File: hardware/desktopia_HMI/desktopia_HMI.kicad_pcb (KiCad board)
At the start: 2 copper layers, 142.2 x 20 mm, 12 parts, among them J1 LCD_Connector, SW1 SW_Push, SW2 SW_Push, SW3 SW_Push, SW4 SW_Push, SW5 SW_Push

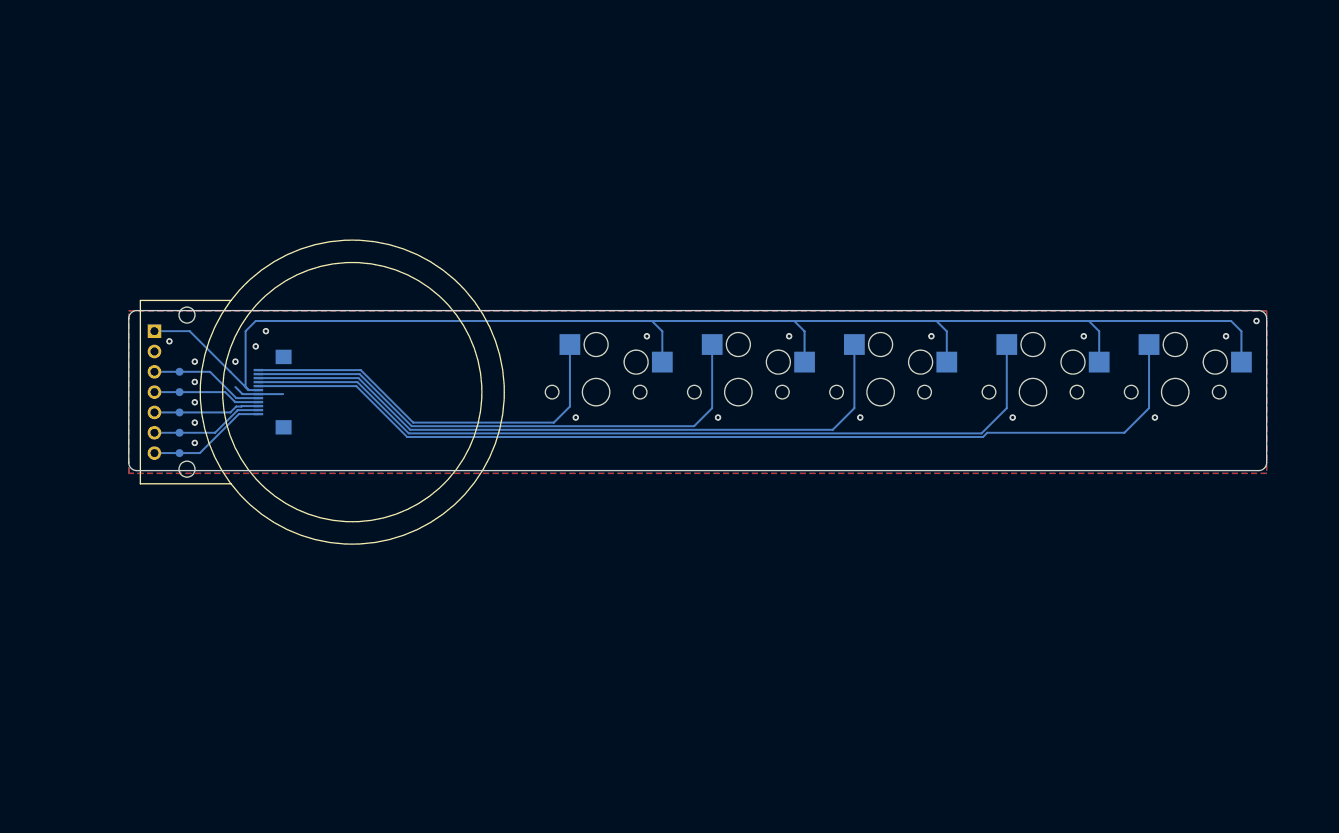
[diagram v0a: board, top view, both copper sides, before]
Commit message: hardware: HMI board re-annotated, PCB updated from the RP2040 schematic
The PCB now holds the RP2040 design (references included); the routing is not finished. README tables, connector pin-outs, test points and assembly notes follow the new references.

Co-Authored-By: Claude Opus 5.5 <noreply@anthropic.com>
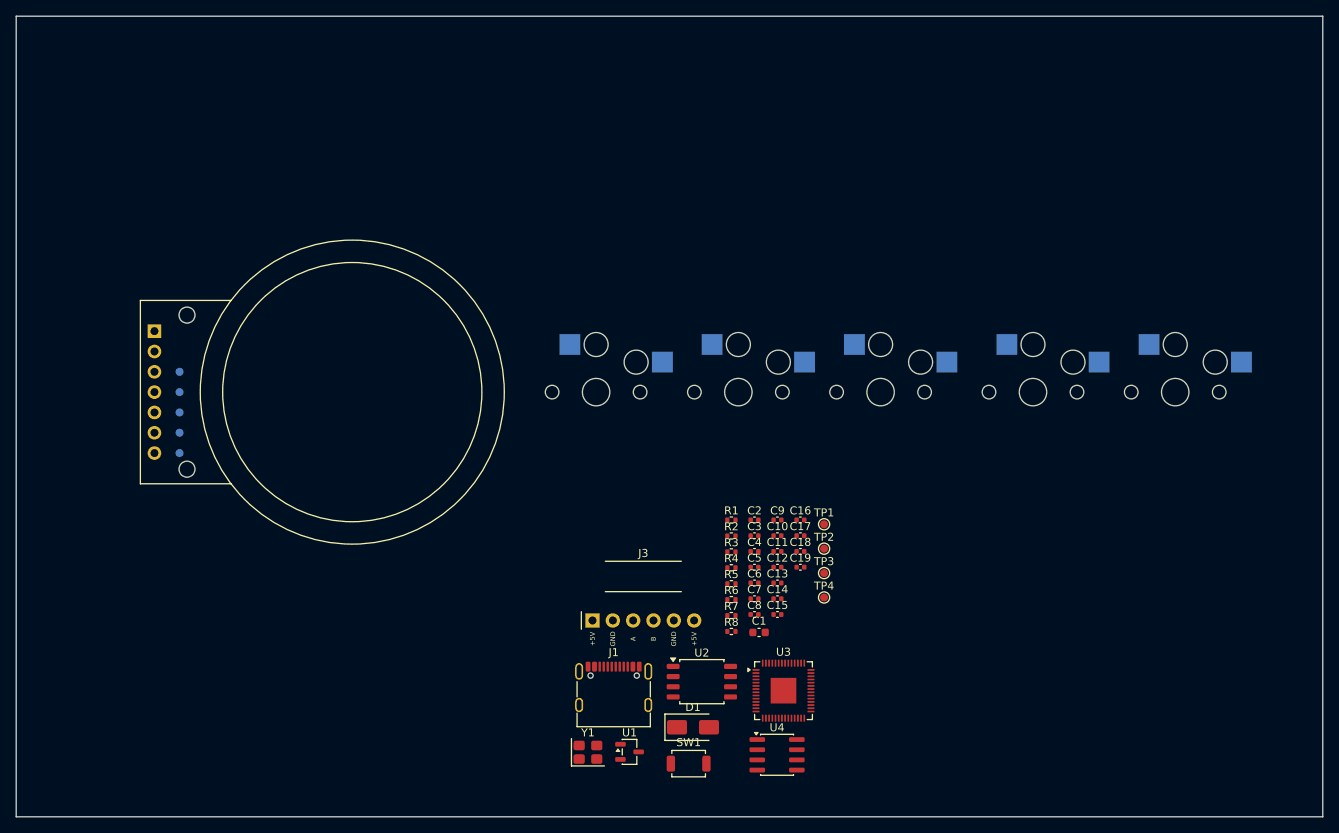
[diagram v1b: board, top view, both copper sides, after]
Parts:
- removed FPC_HMI1: F2D12U-A1G1-ER, JLCImport:F2D12U-A1G1-ER
- added C1: 10uF, Capacitor_SMD:C_0603_1608Metric, F.Cu at (138.6, 117.7)
- added C10: 33pF, Capacitor_SMD:C_0402_1005Metric, F.Cu at (140.9, 105.6)
- added C11: 100nF, Capacitor_SMD:C_0402_1005Metric, F.Cu at (140.9, 107.5)
- added C12: 100nF, Capacitor_SMD:C_0402_1005Metric, F.Cu at (140.9, 109.5)
- added C13: 100nF, Capacitor_SMD:C_0402_1005Metric, F.Cu at (140.9, 111.5)
- added C14: 1uF, Capacitor_SMD:C_0402_1005Metric, F.Cu at (140.9, 113.5)
- added C15: 100nF, Capacitor_SMD:C_0402_1005Metric, F.Cu at (140.9, 115.4)
- added C16: 1uF, Capacitor_SMD:C_0402_1005Metric, F.Cu at (143.7, 103.6)
- added C17: 100nF, Capacitor_SMD:C_0402_1005Metric, F.Cu at (143.7, 105.6)
- added C18: 100nF, Capacitor_SMD:C_0402_1005Metric, F.Cu at (143.7, 107.5)
- added C19: 100nF, Capacitor_SMD:C_0402_1005Metric, F.Cu at (143.7, 109.5)
- added C2: 1uF, Capacitor_SMD:C_0402_1005Metric, F.Cu at (138.0, 103.6)
- added C3: 1uF, Capacitor_SMD:C_0402_1005Metric, F.Cu at (138.0, 105.6)
- added C4: 100nF, Capacitor_SMD:C_0402_1005Metric, F.Cu at (138.0, 107.5)
- added C5: 100nF, Capacitor_SMD:C_0402_1005Metric, F.Cu at (138.0, 109.5)
- added C6: 100nF, Capacitor_SMD:C_0402_1005Metric, F.Cu at (138.0, 111.5)
- added C7: 100nF, Capacitor_SMD:C_0402_1005Metric, F.Cu at (138.0, 113.5)
- added C8: 33pF, Capacitor_SMD:C_0402_1005Metric, F.Cu at (138.0, 115.4)
- added C9: 100nF, Capacitor_SMD:C_0402_1005Metric, F.Cu at (140.9, 103.6)
- added D1: SS14, Diode_SMD:D_SMA, F.Cu at (130.3, 129.5)
- added J1: GT-USB-7010ASV, Connector_USB:USB_C_Receptacle_G-Switch_GT-USB-7010ASV, F.Cu at (120.4, 125.7)
- added J3: 6P6C cord, soldered, Desktopia:Cable_6P6C_SolderPads, F.Cu at (124.1, 116.2)
- added R1: 5.1k, Resistor_SMD:R_0402_1005Metric, F.Cu at (135.1, 103.6)
- added R2: 22, Resistor_SMD:R_0402_1005Metric, F.Cu at (135.1, 105.6)
- added R3: 5.1k, Resistor_SMD:R_0402_1005Metric, F.Cu at (135.1, 107.6)
- added R4: 22, Resistor_SMD:R_0402_1005Metric, F.Cu at (135.1, 109.6)
- added R5: 1k, Resistor_SMD:R_0402_1005Metric, F.Cu at (135.1, 111.6)
- added R6: 1k, Resistor_SMD:R_0402_1005Metric, F.Cu at (135.1, 113.6)
- added R7: 10k, Resistor_SMD:R_0402_1005Metric, F.Cu at (135.1, 115.6)
- added R8: 120, Resistor_SMD:R_0402_1005Metric, F.Cu at (135.1, 117.5)
- added SW1: TS-1088-AR02016, Button_Switch_SMD:SW_SPST_TS-1088-xR020, F.Cu at (129.8, 134.1)
- added TP1: TestPoint, TestPoint:TestPoint_Pad_D1.0mm, F.Cu at (146.7, 104.1)
- added TP2: TestPoint, TestPoint:TestPoint_Pad_D1.0mm, F.Cu at (146.7, 107.2)
- added TP3: TestPoint, TestPoint:TestPoint_Pad_D1.0mm, F.Cu at (146.7, 110.2)
- added TP4: TestPoint, TestPoint:TestPoint_Pad_D1.0mm, F.Cu at (146.7, 113.3)
- added U1: XC6206P332MR, Package_TO_SOT_SMD:SOT-23-3, F.Cu at (122.4, 132.6)
- added U2: W25Q128JVSIQ, Package_SO:SOIC-8_5.3x5.3mm_P1.27mm, F.Cu at (131.4, 123.8)
- added U3: RP2040, Package_DFN_QFN:QFN-56-1EP_7x7mm_P0.4mm_EP3.2x3.2mm, F.Cu at (141.6, 124.9)
- added U4: SP3485EN-L/TR, Package_SO:SOIC-8_3.9x4.9mm_P1.27mm, F.Cu at (140.8, 133.0)
- added Y1: 12MHz, Crystal:Crystal_SMD_3225-4Pin_3.2x2.5mm, F.Cu at (117.2, 132.6)
- renumbered J1 to J2, SW1 to SW2, SW2 to SW3, SW3 to SW4, SW4 to SW5, SW5 to SW6, TP2 to TP5, TP3 to TP6, TP4 to TP7, TP5 to TP8, TP6 to TP9
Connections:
- net /MOSI_HMIside renamed Net-(J2-Pin_4)
- J2 pad 1: +5VA -> Net-(J2-Pin_1)
- J2 pad 2: GNDA -> Net-(J2-Pin_2)
- J2 pad 3: /SCK_HMIside -> Net-(J2-Pin_3)
- J2 pad 5: /DC_HMIside -> Net-(J2-Pin_5)
- J2 pad 6: /CS_HMIside -> GND
- J2 pad 7: /RST_HMIside -> +5V
- SW2 pad 1: /SW1_HMIside -> Net-(U3-GPIO11)
- SW2 pad 2: +5VA -> GND
- SW3 pad 1: /SW2_HMIside -> Net-(U3-GPIO12)
- SW3 pad 2: +5VA -> GND
- SW4 pad 1: /SW3_HMIside -> Net-(U3-GPIO13)
- SW4 pad 2: +5VA -> GND
- SW5 pad 1: /SW4_HMIside -> Net-(U3-GPIO14)
- SW5 pad 2: +5VA -> GND
- SW6 pad 1: /SW5_HMIside -> Net-(U3-GPIO15)
- SW6 pad 2: +5VA -> GND
- TP5 pad 1: /SCK_HMIside -> Net-(J2-Pin_5)
- TP7 pad 1: /DC_HMIside -> Net-(J2-Pin_3)
- TP8 pad 1: /CS_HMIside -> Net-(J2-Pin_2)
- TP9 pad 1: /RST_HMIside -> Net-(J2-Pin_1)
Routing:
- net +5VA: track 175.7 -> 0.00 mm
- net /SW5_HMIside: track 123.4 -> 0.00 mm
- net /SW4_HMIside: track 105.5 -> 0.00 mm
- net /SW3_HMIside: track 86.3 -> 0.00 mm
- net /SW2_HMIside: track 68.3 -> 0.00 mm
- net /SW1_HMIside: track 50.2 -> 0.00 mm
- net /RST_HMIside: track 15.0 -> 0.00 mm
- net /SCK_HMIside: track 14.4 -> 0.00 mm
- net /CS_HMIside: track 14.2 -> 0.00 mm
- net Net-(J2-Pin_4): track 13.5 -> 0.00 mm
- net /DC_HMIside: track 13.3 -> 0.00 mm
- net GNDA: track 6.33 -> 0.00 mm, vias 20 -> 0
- removed copper zone on B.Cu, net GNDA
- removed copper zone on F.Cu, net GNDA
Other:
- board size 142.2 x 20 mm -> 163.3 x 100.1 mm
